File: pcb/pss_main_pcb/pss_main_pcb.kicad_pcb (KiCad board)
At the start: 2 copper layers, 177.8 x 55.9 mm, 96 parts, among them J1 24V DC Input, J2 220V AC Input, J3 Hot Air Gun, J4 Soldering Iron, J5 STM32_Prog, J6 UART_Prog, Q1 BC817, Q2 MMBT2222, Q3 MMBT2907, Q4 IRLML9301T, Q5 IRFZ44S, Q6 BT139B-800, SW1 Hot Air Gun Input, SW2 Soldering Iron Input, SW3 SW_Push, SW4 Main Encoder Input, SW5 EN, SW6 Boot, U1 LM2596S-5, U2 LM2596S-3.3, U3 MOC3023S, U4 LM358, U5 STM32F030K6Tx, U6 ESP32-WROOM-32U, U7 2.8inch_SPI_Module_ILI9341_SK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

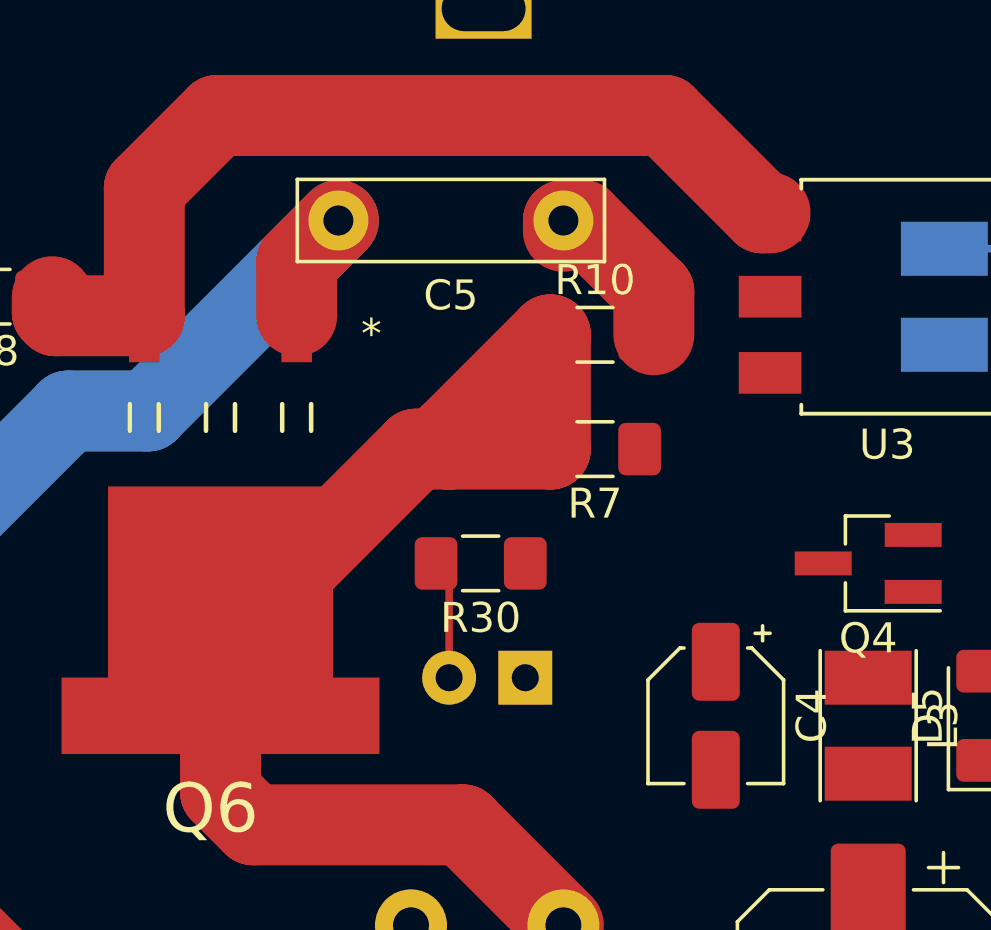
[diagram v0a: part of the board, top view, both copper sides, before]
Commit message: Change routing
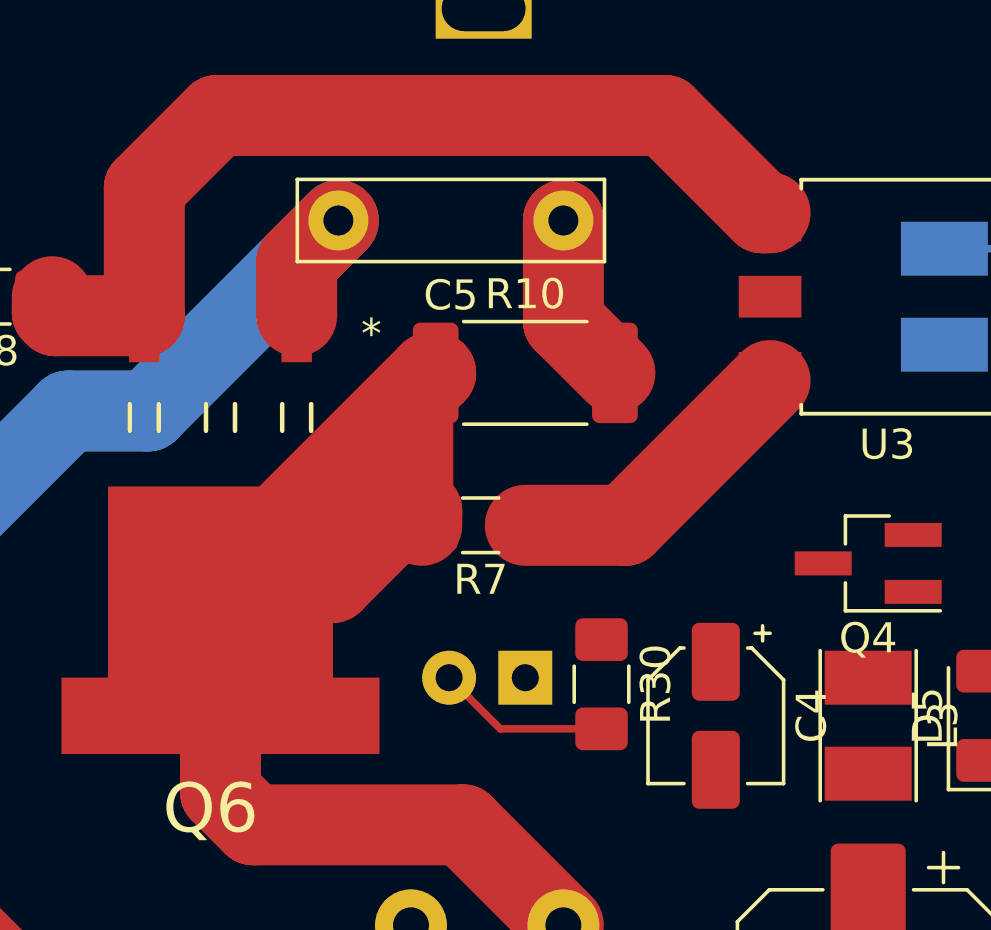
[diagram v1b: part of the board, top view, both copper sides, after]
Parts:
- R10: footprint Resistor_SMD:R_1206_3216Metric_Pad1.42x1.75mm_HandSolder -> Resistor_SMD:R_2512_6332Metric_Pad1.52x3.35mm_HandSolder
- moved R30 5.70 mm to (88.9, 98.0), turned to 270 degrees
- moved R7 4.58 mm to (84.9, 92.7)
- moved R10 2.65 mm to (86.4, 87.6)
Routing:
- net Net-(R7-Pad1): track 0.00 -> 10.2 mm
- net 220V_Heater1: track 42.1 -> 45.4 mm
- net Net-(D8-Pad2): track 3.99 -> 5.79 mm

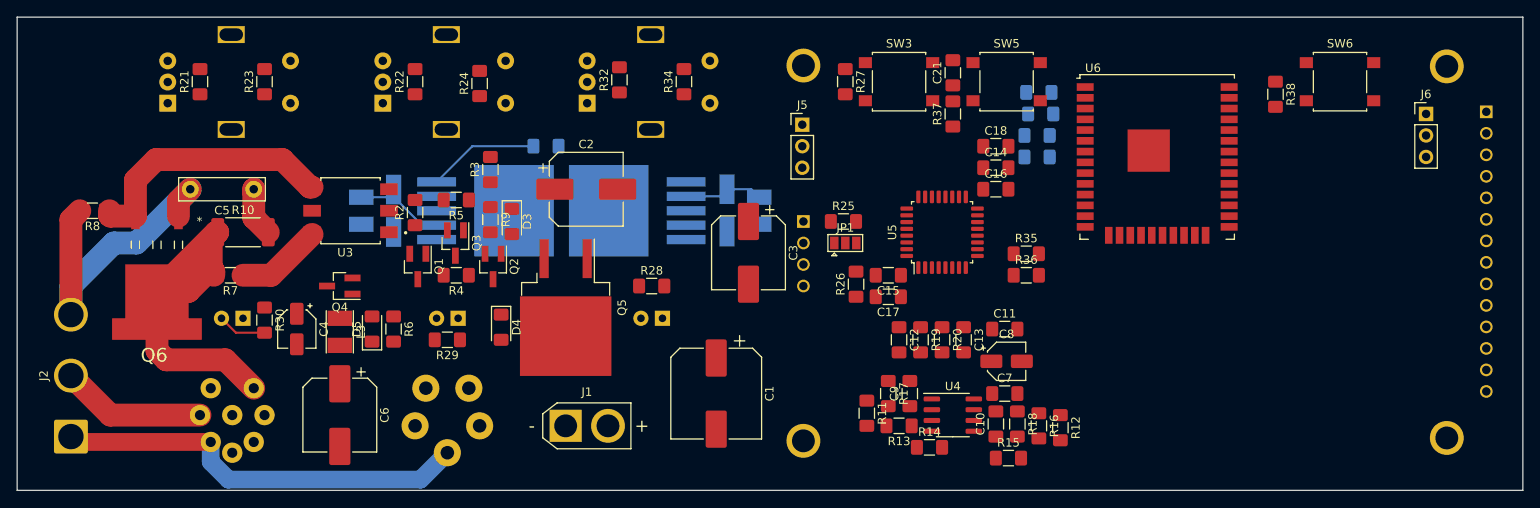
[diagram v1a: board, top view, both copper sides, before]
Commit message: Add new routes
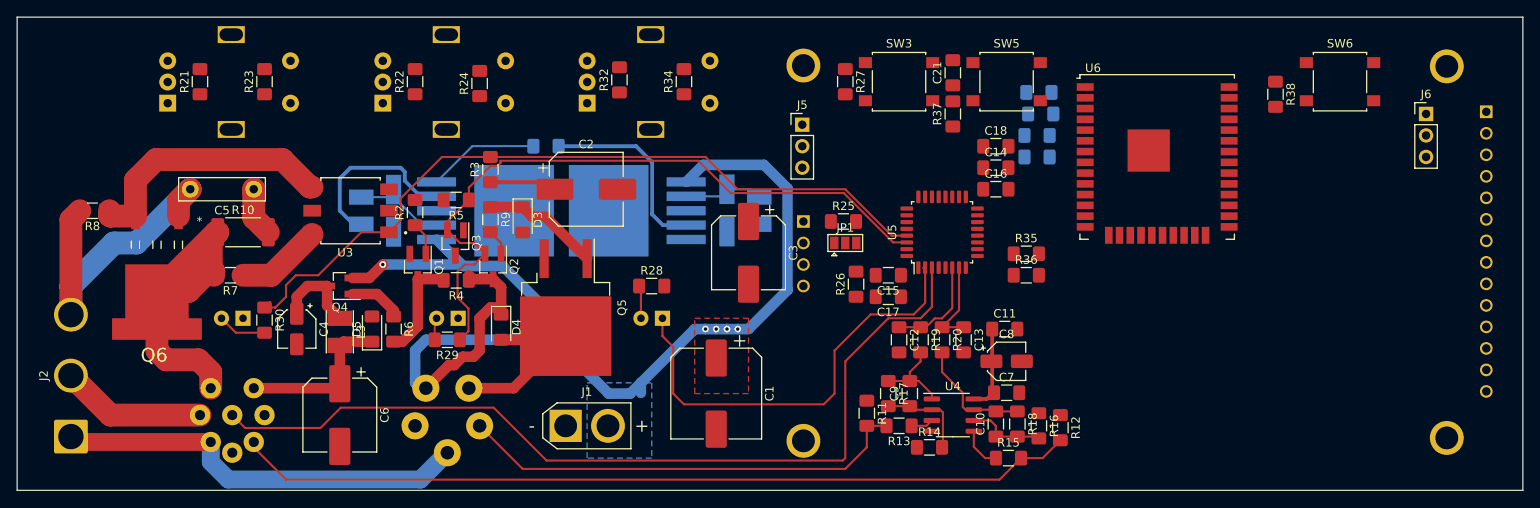
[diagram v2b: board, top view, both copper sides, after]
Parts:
- moved D3 1.29 mm to (119.4, 86.2)
- moved R4 0.60 mm to (111.5, 93.3)
- moved C7 0.24 mm to (176.5, 106.6)
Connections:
- J3 pad 1: 220V_Heater1 -> Hot_Air_Fan
- J3 pad 3: Hot_Air_Reed -> Hot_Air_Therm_Pos
- J3 pad 7: Hot_Air_Fan -> 220V_Heater1
- J3 pad 8: Hot_Air_Therm_Pos -> Hot_Air_Reed
- J4 pad 1: Iron_Heat_Pos -> Iron_Heat_Neg
- J4 pad 2: Iron_Heat_Neg -> Iron_Therm_Pos
- J4 pad 5: Iron_Therm_Pos -> Iron_Heat_Pos
- U5 pad 25: Hot_Air_Reed -> Net-(U5-Pad25)
- U5 pad 3: Net-(U5-Pad3) -> Hot_Air_Reed
- U5 pad 6: Hot_Air_Themp_ADC -> Iron_Themp_ADC
- U5 pad 7: Iron_Themp_ADC -> Hot_Air_Themp_ADC
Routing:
- net Iron_Heat_Pos: track 0.00 -> 140.3 mm, vias 0 -> 5
- net Hot_Air_Reed: track 0.00 -> 105.8 mm
- net Hot_Air_Therm_Pos: track 0.00 -> 99.4 mm
- net Heater_PWM: track 0.00 -> 90.3 mm
- net Sold_PWM: track 0.00 -> 82.1 mm
- net Iron_Therm_Pos: track 0.00 -> 53.7 mm
- net Enable_5V: track 13.2 -> 65.9 mm
- net +3V3: track 0.00 -> 32.7 mm
- net +5V: track 1.74 -> 30.7 mm
- net Iron_Heat_Neg: track 0.00 -> 21.8 mm
- net Hot_Air_Fan: track 0.00 -> 18.9 mm
- net Net-(C10-Pad2): track 0.00 -> 14.1 mm
- net Net-(D3-Pad1): track 0.00 -> 14.0 mm
- net Net-(Q1-Pad3): track 0.00 -> 12.3 mm
- net Iron_Themp_ADC: track 0.00 -> 12.0 mm
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- added copper zone on B.Cu, net Iron_Heat_Pos
- added copper zone on F.Cu, net Iron_Heat_Pos
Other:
- net class Power_220: clearance 0.75 -> 0.5
- net class Power_24 added: clearance 0.5, trace_width 1.25, via_dia 0.8, via_drill 0.4
- net class Power_3_3_5 added: clearance 0.2, trace_width 0.45, via_dia 0.8, via_drill 0.4

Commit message: Add routes for low power rails
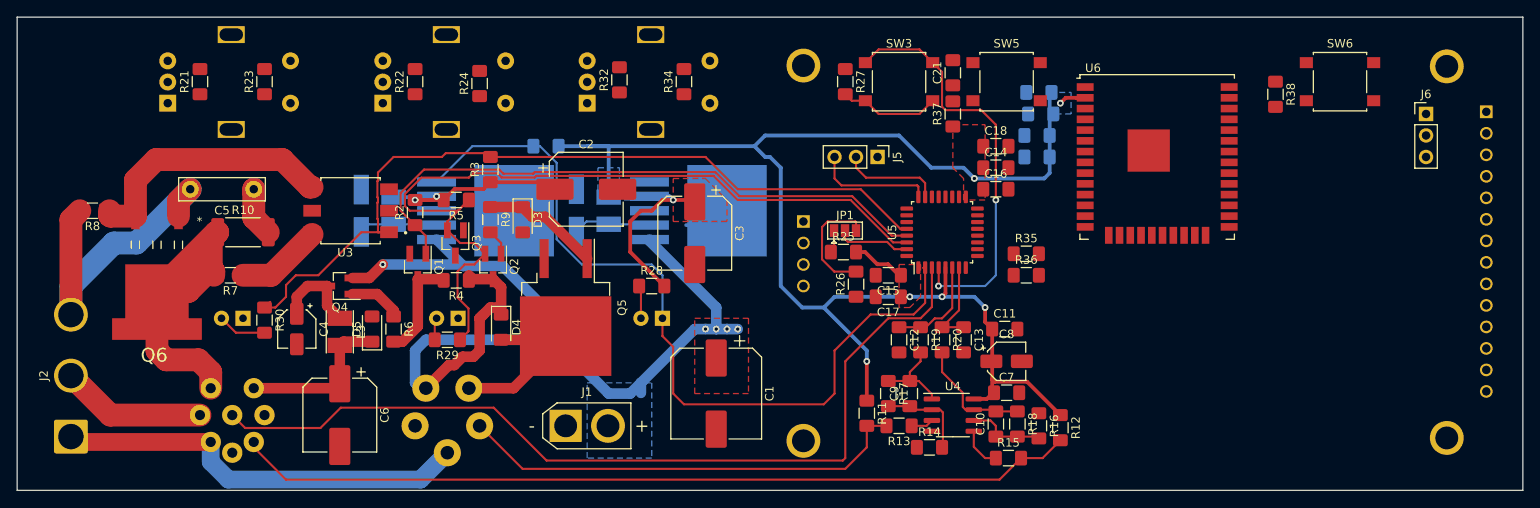
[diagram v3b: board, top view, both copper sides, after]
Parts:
- moved L2 17.8 mm to (129.5, 85.1), turned to 270 degrees
- moved D2 17.8 mm to (125.7, 85.0), turned to 90 degrees
- moved J5 9.67 mm to (161.3, 78.7), turned to 270 degrees
- moved U2 7.22 mm to (140.1, 85.1), turned to 0 degrees
- moved C3 6.76 mm to (139.7, 87.7)
- moved D1 3.81 mm to (100.3, 85.1), turned to 90 degrees
- moved L1 3.81 mm to (104.1, 85.1), turned to 270 degrees
- moved R25 3.61 mm to (157.3, 90.0)
- moved JP1 1.47 mm to (157.4, 87.4)
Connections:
- U5 pad 21: Fan_PWM -> Net-(U5-Pad21)
- U5 pad 28: Net-(U5-Pad28) -> Heater_PWM
- U5 pad 29: Heater_PWM -> Fan_PWM
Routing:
- net +3V3: track 32.7 -> 201.7 mm, vias 0 -> 7
- net Fan_PWM: track 3.90 -> 72.7 mm
- net STM_RST: track 0.00 -> 49.4 mm, vias 0 -> 2
- net Enable_5V: track 65.9 -> 97.8 mm
- net Iron_Heat_Pos: track 140.3 -> 120.0 mm
- net Sold_PWM: track 82.1 -> 97.0 mm
- net STM_SWCLK: track 0.00 -> 14.1 mm
- net Net-(JP1-Pad3): track 0.00 -> 13.7 mm
- net Net-(R27-Pad2): track 0.00 -> 11.9 mm
- net STM_SWDIO: track 0.00 -> 11.8 mm
- net STM_BOOT: track 0.00 -> 8.78 mm
- net Heater_PWM: track 90.3 -> 95.7 mm
- net GND: track 0.00 -> 3.24 mm
- net Net-(JP1-Pad1): track 0.00 -> 2.70 mm
- net +5V: track 30.7 -> 29.4 mm, vias 0 -> 2
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- added copper zone on B.Cu, net +3V3
- added copper zone on F.Cu, net +3V3

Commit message: Change routes
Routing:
- net Net-(R38-Pad1): track 0.00 -> 13.8 mm
- net EN: track 0.00 -> 9.24 mm
- net GND: track 3.24 -> 12.5 mm
- net Net-(R22-Pad1): track 0.00 -> 4.41 mm
- net Net-(R21-Pad1): track 0.00 -> 4.41 mm
- net Net-(R32-Pad1): track 0.00 -> 4.32 mm
- net Net-(Q2-Pad1): track 3.39 -> 7.41 mm
- net Net-(R23-Pad1): track 0.00 -> 3.51 mm
- net Net-(R34-Pad1): track 0.00 -> 3.51 mm
- net Net-(R24-Pad1): track 0.00 -> 3.42 mm
- net Net-(D3-Pad1): track 14.0 -> 15.8 mm

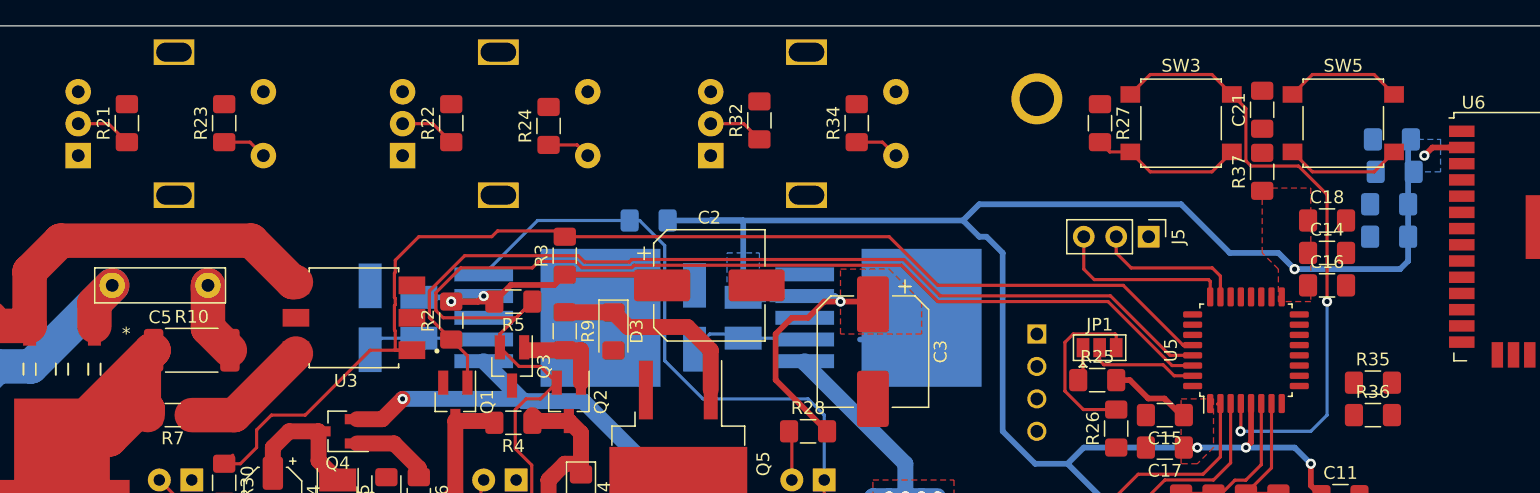
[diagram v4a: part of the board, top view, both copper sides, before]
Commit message: Add encoders routes
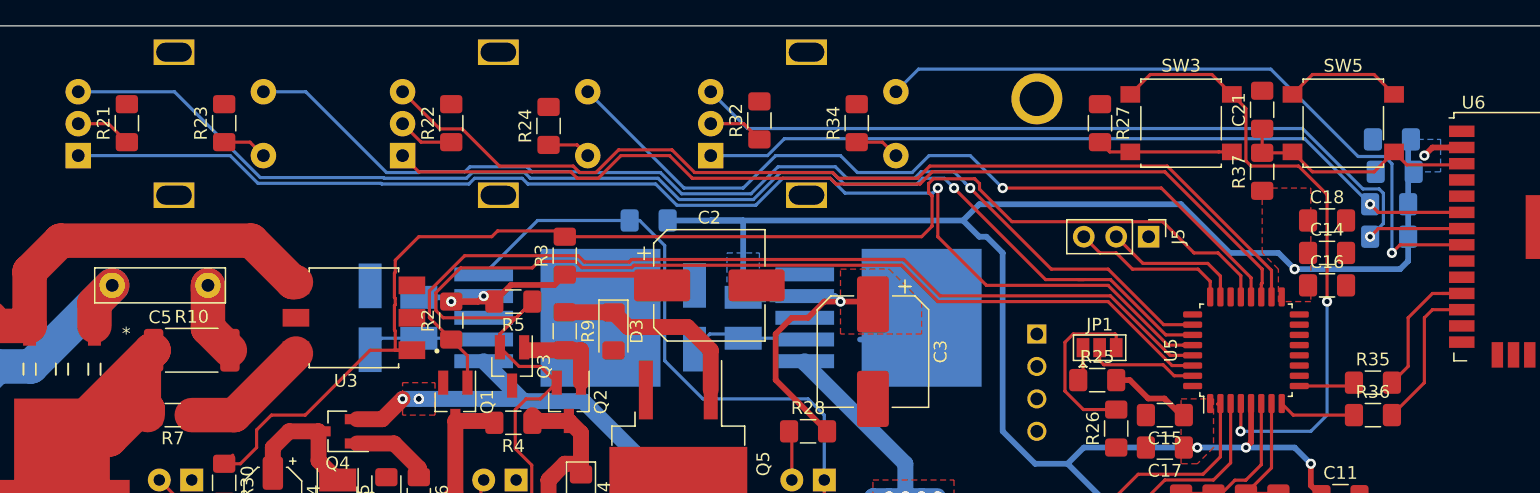
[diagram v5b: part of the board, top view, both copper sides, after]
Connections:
- U5 pad 11: Sold_Switch -> Net-(U5-Pad11)
- U5 pad 12: Sold_Enc_A -> Net-(U5-Pad12)
- U5 pad 13: Sold_Enc_B -> Net-(U5-Pad13)
- U5 pad 18: HotA_Enc_A -> Sold_Enc_B
- U5 pad 19: HotA_Enc_B -> Sold_Enc_A
- U5 pad 20: HotA_Switch -> Sold_Switch
- U5 pad 21: Net-(U5-Pad21) -> Heater_PWM
- U5 pad 26: Net-(U5-Pad26) -> HotA_Switch
- U5 pad 27: Net-(U5-Pad27) -> HotA_Enc_B
- U5 pad 28: Heater_PWM -> HotA_Enc_A
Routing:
- net HotA_Enc_A: track 0.00 -> 98.9 mm, vias 0 -> 1
- net HotA_Enc_B: track 0.00 -> 98.1 mm, vias 0 -> 1
- net HotA_Switch: track 0.00 -> 82.9 mm, vias 0 -> 1
- net Sold_Enc_B: track 0.00 -> 78.2 mm
- net Sold_Enc_A: track 0.00 -> 75.5 mm
- net Main_Enc_B: track 0.00 -> 67.2 mm, vias 0 -> 1
- net Sold_Switch: track 0.00 -> 62.7 mm, vias 0 -> 1
- net Main_Enc_A: track 0.00 -> 61.7 mm, vias 0 -> 1
- net Main_Switch: track 0.00 -> 55.4 mm, vias 0 -> 1
- net ESP32_UART_TX: track 0.00 -> 12.2 mm
- net ESP32_UART_RX: track 0.00 -> 11.9 mm
- net EN: track 9.24 -> 19.3 mm
- net Heater_PWM: track 95.7 -> 105.2 mm
- net STM_UART_TX: track 0.00 -> 6.03 mm
- net STM_UART_RX: track 0.00 -> 4.39 mm
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
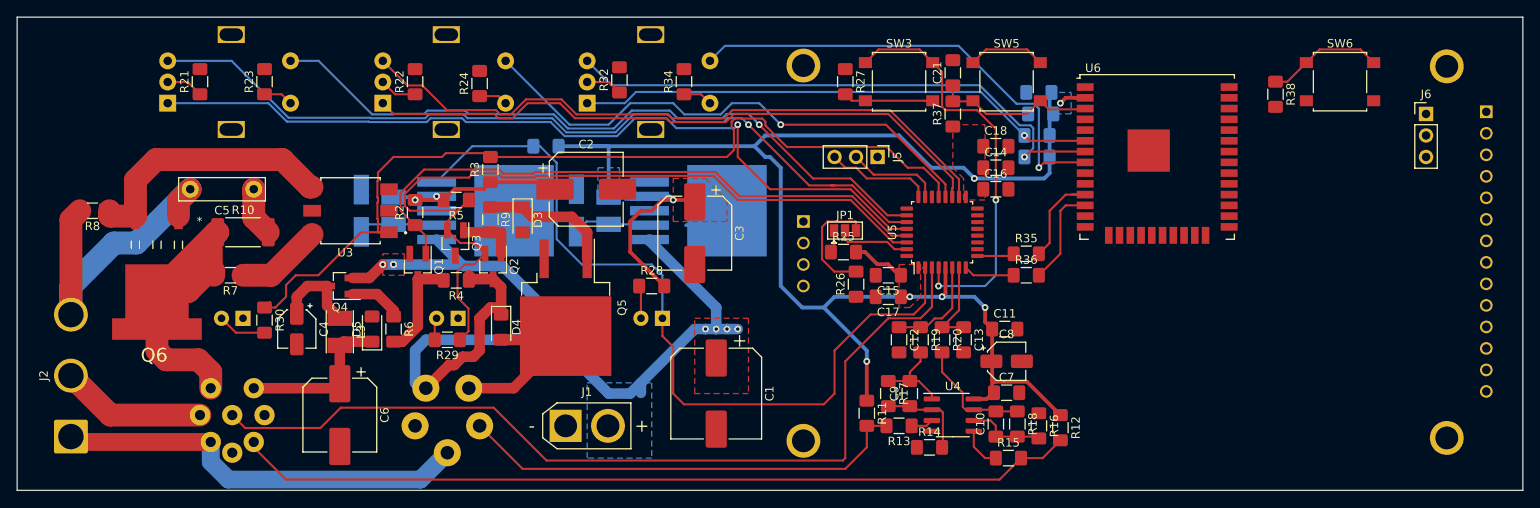
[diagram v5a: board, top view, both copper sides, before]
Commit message: Add routes and fill planes
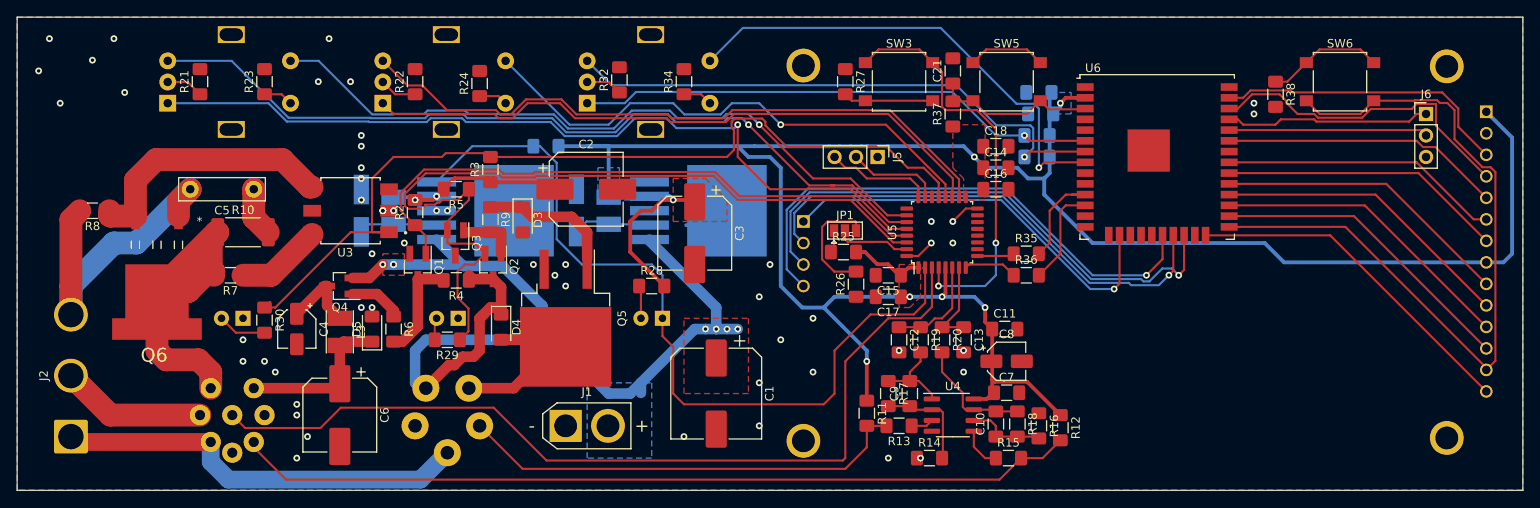
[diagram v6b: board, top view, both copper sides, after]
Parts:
- moved Q5 1.27 mm to (124.5, 97.8)
- moved R14 1.27 mm to (167.4, 114.3)
- moved R5 1.27 mm to (111.5, 82.5)
- moved C21 0.22 mm to (170.2, 68.6)
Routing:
- net Boot: track 0.00 -> 90.5 mm
- net +3V3: track 201.7 -> 285.6 mm
- net SD_SDO: track 0.00 -> 64.0 mm, vias 0 -> 1
- net SD_SCK: track 0.00 -> 63.1 mm, vias 0 -> 1
- net SD_SDI: track 0.00 -> 58.8 mm, vias 0 -> 1
- net SD_CS: track 0.00 -> 48.7 mm, vias 0 -> 1
- net DISP_T_IRQ: track 0.00 -> 40.8 mm
- net DISP_RST: track 0.00 -> 38.0 mm
- net DISP_T_DIN: track 0.00 -> 36.8 mm
- net DISP_T_CS: track 0.00 -> 36.3 mm
- net DISP_T_CLK: track 0.00 -> 35.8 mm
- net DISP_SDO: track 0.00 -> 35.3 mm
- net DISP_CS: track 0.00 -> 35.1 mm
- net DISP_SCK: track 0.00 -> 33.7 mm
- net DISP_DC_RS: track 0.00 -> 33.2 mm
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- added copper zone on B.Cu, net GND
- added copper zone on F.Cu, net GND
